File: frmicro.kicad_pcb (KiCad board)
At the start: 2 copper layers, 25 x 33.7 mm, 20 parts, among them J1 Conn_01x12_Female, J2 Conn_01x12_Female, P2 USB_C_Plug, SW1 SW_Push, U1 ATmega32U4-AU, Y1 16Mhz

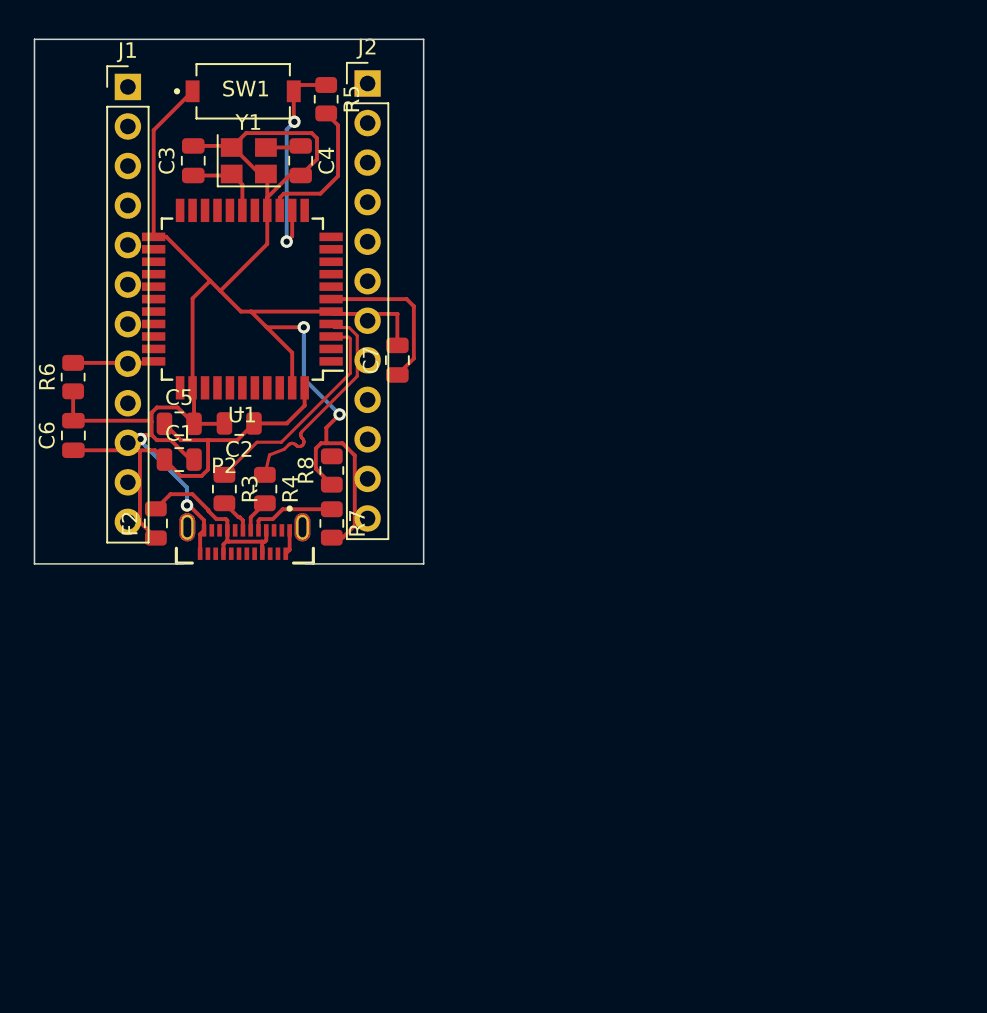
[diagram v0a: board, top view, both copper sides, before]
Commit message: add pro micro schematics and work from that.
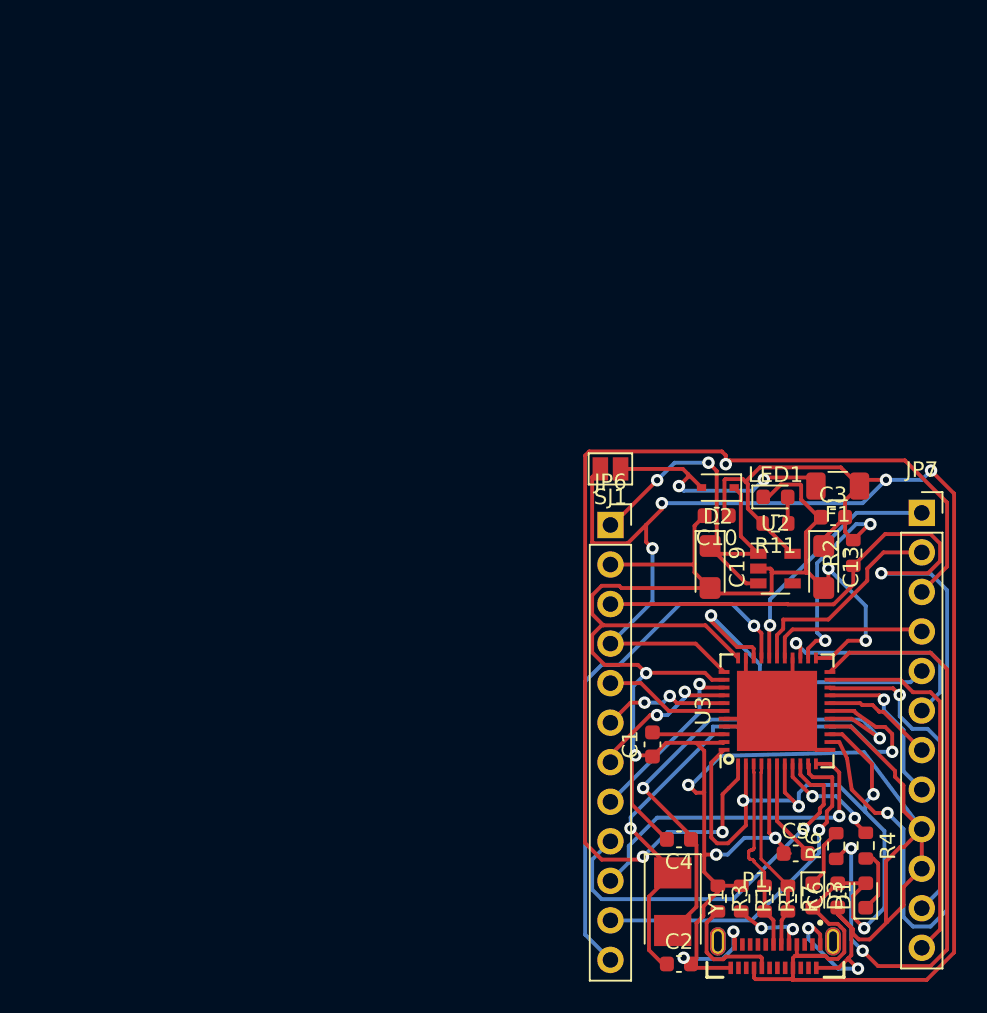
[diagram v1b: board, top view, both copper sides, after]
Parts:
- removed C7: 1uF, Capacitor_SMD:C_0805_2012Metric
- removed F2: Polyfuse_Small, Fuse:Fuse_0805_2012Metric
- removed J1, J2: Conn_01x12_Female, Connector_PinHeader_2.54mm:PinHeader_1x12_P2.54mm_Vertical
- removed P2: USB_C_Plug, misc:GCT_USB4155-03-C_REVA
- removed R8: 5.1k, Resistor_SMD:R_0805_2012Metric
- removed SW1: SW_Push, misc:SW_PTS636_SM43J_SMTR_LFS
- removed U1: ATmega32U4-AU, Package_QFP:TQFP-44_10x10mm_P0.8mm
- added C10: 1uF, Capacitor_SMD:C_0603_1608Metric, F.Cu at (103.8, 80.6)
- added C13: 10uF, Capacitor_Tantalum_SMD:CP_EIA-3216-18_Kemet-A, F.Cu at (110.7, 83.9)
- added C19: 10uF, Capacitor_Tantalum_SMD:CP_EIA-3216-18_Kemet-A, F.Cu at (103.4, 83.9)
- added D1: Yellow, LED_SMD:LED_0603_1608Metric, F.Cu at (113.4, 105.0)
- added D2: DIODESOD, Diode_SMD:D_SOD-323, F.Cu at (103.9, 78.8)
- added D3: Green, LED_SMD:LED_0603_1608Metric, F.Cu at (110.0, 105.0)
- added F1: 500mA, Fuse:Fuse_1206_3216Metric, F.Cu at (111.6, 78.7)
- added JP6: M12PTH, Connector_PinSocket_2.54mm:PinSocket_1x12_P2.54mm_Vertical, F.Cu at (97.0, 81.2)
- added JP7: M12PTH, Connector_PinSocket_2.54mm:PinSocket_1x12_P2.54mm_Vertical, F.Cu at (117.0, 80.4)
- added LED1: Red, LED_SMD:LED_0603_1608Metric, F.Cu at (107.6, 79.4)
- added P1: USB_C_Plug, misc:GCT_USB4155-03-C_REVA, F.Cu at (107.6, 108.9)
- added R1: 22, Resistor_SMD:R_0603_1608Metric, F.Cu at (105.4, 105.2)
- added R11: 1K, Resistor_SMD:R_0603_1608Metric, F.Cu at (107.6, 81.1)
- added R2: 10K, Resistor_SMD:R_0603_1608Metric, F.Cu at (112.6, 83.0)
- added SJ1: Closed for 5V Board, Jumper:SolderJumper-2_P1.3mm_Open_Pad1.0x1.5mm, F.Cu at (97.0, 77.6)
- added U2: MIC5219, Package_TO_SOT_SMD:SOT-23-5, F.Cu at (107.6, 84.0)
- added U3: ATMEGA32U4, misc:QFN-44-1EP_7x7mm_Pitch0.5mm, F.Cu at (107.7, 93.1)
- C1, C4: footprint Capacitor_SMD:C_0805_2012Metric -> Capacitor_SMD:C_0603_1608Metric
- C2: value 0.1uF -> 22pF; footprint Capacitor_SMD:C_0805_2012Metric -> Capacitor_SMD:C_0603_1608Metric
- C3: value 22pF -> 0.1uF; footprint Capacitor_SMD:C_0805_2012Metric -> Capacitor_SMD:C_0603_1608Metric
- C5, C6: value 0.1uF -> 1uF; footprint Capacitor_SMD:C_0805_2012Metric -> Capacitor_SMD:C_0603_1608Metric
- R3: footprint Resistor_SMD:R_0805_2012Metric -> Resistor_SMD:R_0603_1608Metric
- R4: value 22 -> 330; footprint Resistor_SMD:R_0805_2012Metric -> Resistor_SMD:R_0603_1608Metric
- R5: value 10k -> 22; footprint Resistor_SMD:R_0805_2012Metric -> Resistor_SMD:R_0603_1608Metric
- R6: value 10k -> 330; footprint Resistor_SMD:R_0805_2012Metric -> Resistor_SMD:R_0603_1608Metric
- R7: value 5.1k -> 22; footprint Resistor_SMD:R_0805_2012Metric -> Resistor_SMD:R_0603_1608Metric
- Y1: value 16Mhz -> 16MHz; footprint Crystal:Crystal_SMD_3225-4Pin_3.2x2.5mm -> Crystal:Crystal_SMD_5032-2Pin_5.0x3.2mm
- moved R5 58.6 mm to (106.9, 105.2)
- moved R6 57.5 mm to (111.5, 101.8)
- moved C6 57.3 mm to (111.6, 105.0)
- moved Y1 54.8 mm to (101.0, 105.4), turned to 270 degrees
- moved C4 49.9 mm to (101.4, 101.4), turned to 180 degrees
- moved C5 48.3 mm to (108.9, 102.3)
- moved C3 47.0 mm to (111.3, 80.7), turned to 0 degrees
- moved R4 44.9 mm to (113.4, 101.8)
- moved C2 44.8 mm to (101.4, 109.4), turned to 0 degrees
- moved R3 41.2 mm to (103.9, 105.2)
- moved R7 37.9 mm to (108.4, 105.2)
- moved C1 35.5 mm to (99.7, 95.3), turned to 90 degrees
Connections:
- C1 pad 1: VCC -> GND
- C1 pad 2: GND -> /AREF
- C2 pad 1: VCC -> Net-(C2-Pad1)
- C3 pad 1: Net-(C3-Pad1) -> GND
- C3 pad 2: GND -> 3.3V
- C5 pad 1: VCC -> GND
- C5 pad 2: GND -> Net-(C5-Pad2)
- C6 pad 1: VCC -> GND
- C6 pad 2: GND -> 3.3V
- R3 pad 1: /Dline- -> GND
- R3 pad 2: D- -> Net-(P1-PadB5)
- R4 pad 1: /Dline+ -> /D14
- R4 pad 2: D+ -> Net-(D1-Pad1)
- R5 pad 1: Net-(R5-Pad1) -> /D-
- R5 pad 2: VCC -> /D-
- R6 pad 1: GND -> Net-(R6-Pad1)
- R7 pad 1: Net-(P2-PadA5) -> /D+
- R7 pad 2: GND -> /D+
- Y1 pad 1: Net-(C3-Pad1) -> Net-(C2-Pad1)
- Y1 pad 2: GND -> Net-(C4-Pad1)
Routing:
- net 3.3V: track 0.00 -> 191.6 mm, vias 0 -> 10
- net /RESET: track 0.00 -> 71.8 mm, vias 0 -> 2
- net /D7: track 0.00 -> 71.4 mm, vias 0 -> 3
- net GND: track 124.3 -> 188.3 mm, vias 4 -> 11
- net Net-(R6-Pad1): track 0.00 -> 40.9 mm, vias 0 -> 2
- net VCC: track 38.5 -> 0.00 mm
- net Net-(C2-Pad1): track 0.00 -> 37.8 mm, vias 0 -> 2
- net /D10: track 0.00 -> 34.3 mm, vias 0 -> 1
- net Net-(C4-Pad1): track 2.58 -> 32.4 mm, vias 0 -> 2
- net /RAW: track 0.00 -> 26.0 mm, vias 0 -> 2
- net /SCK: track 0.00 -> 25.1 mm, vias 0 -> 1
- net /TXO: track 0.00 -> 24.0 mm
- net /MOSI: track 0.00 -> 22.7 mm, vias 0 -> 1
- net /MISO: track 0.00 -> 21.6 mm, vias 0 -> 1
- net /RXI: track 0.00 -> 20.5 mm, vias 0 -> 1
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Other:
- board outline removed
